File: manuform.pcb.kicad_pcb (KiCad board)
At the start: 2 copper layers, 89 x 94 mm, 45 parts, among them J1 Conn_01x05, J2 Conn_01x04, J3 Conn_01x01, J4 Conn_01x01, J5 Conn_01x01, SW1 SW_DIP_x01, SW2 SW_DIP_x01, SW3 SW_DIP_x01, SW4 SW_DIP_x01, SW5 SW_DIP_x01

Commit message: added gnd lugs
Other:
- board text added: "v0.0 Flatmax"
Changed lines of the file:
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@@
   (gr_line (start 189.5 28) (end 171.5 28)
     (stroke (width 0.05) (type default)) (layer "Edge.Cuts"))
+  (gr_text "v0.0\n\nFlatmax" (at 138 87.5 90) (layer "F.Cu")
+    (effects (font (size 1.5 1.5) (thickness 0.3) bold) (justify left bottom))
+  )
   (segment (start 154 59.38) (end 156 61.38) (width 0.2) (layer "F.Cu") (net 1))
   (segment (start 163 62.88) (end 164.5 61.38) (width 0.2) (layer "F.Cu") (net 1))

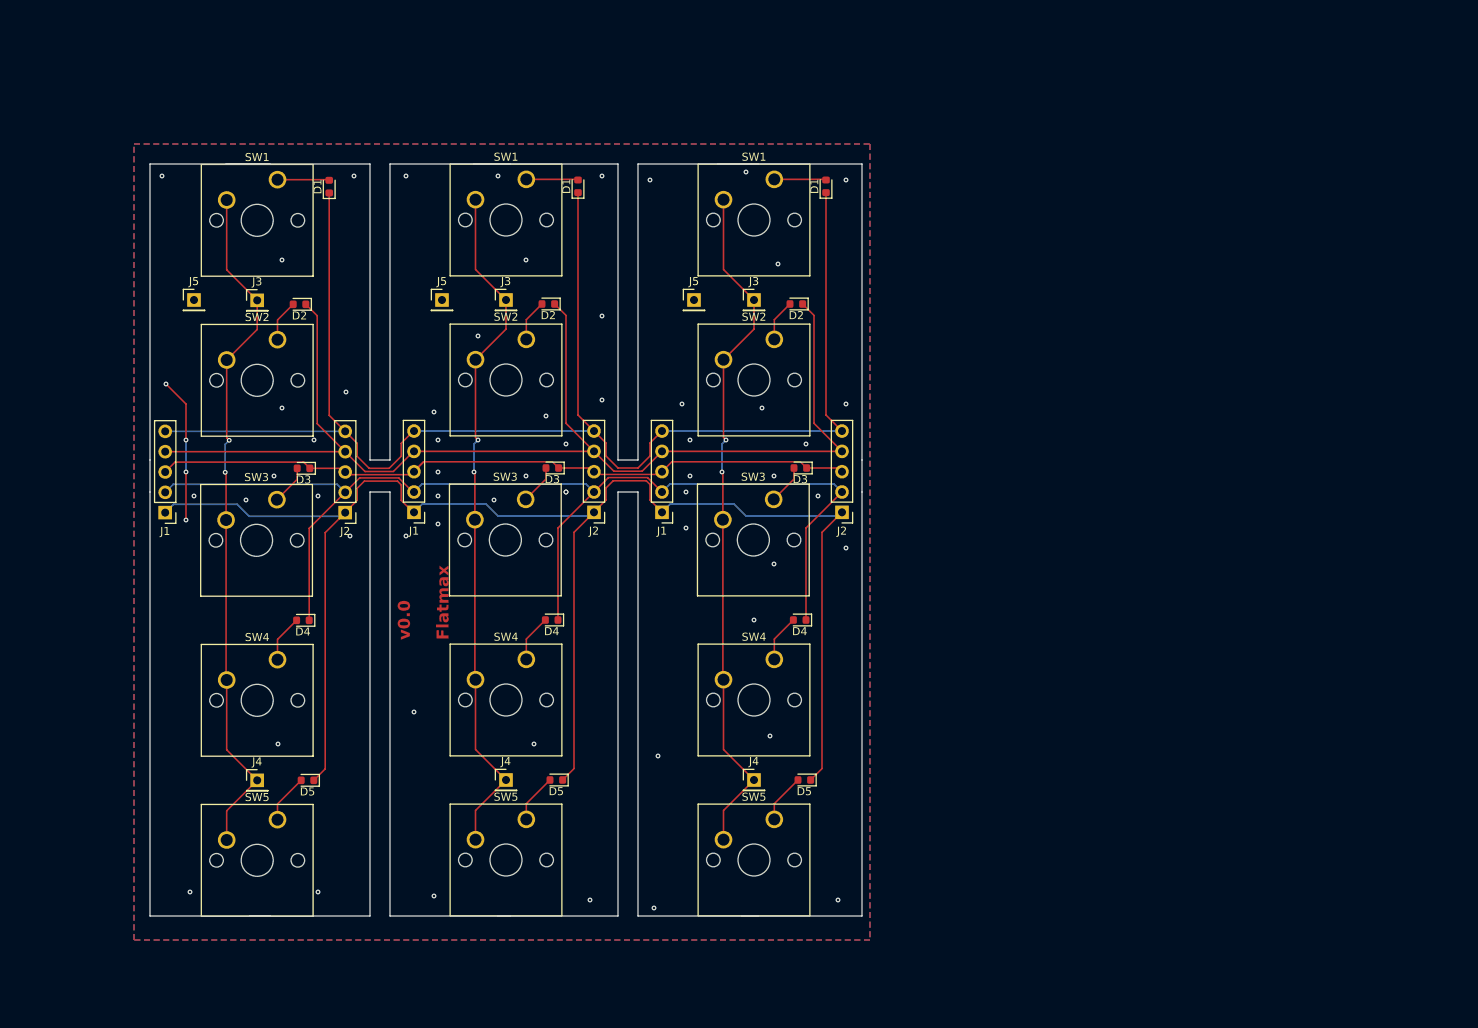
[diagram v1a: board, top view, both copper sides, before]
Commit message: increased separation to 25mm
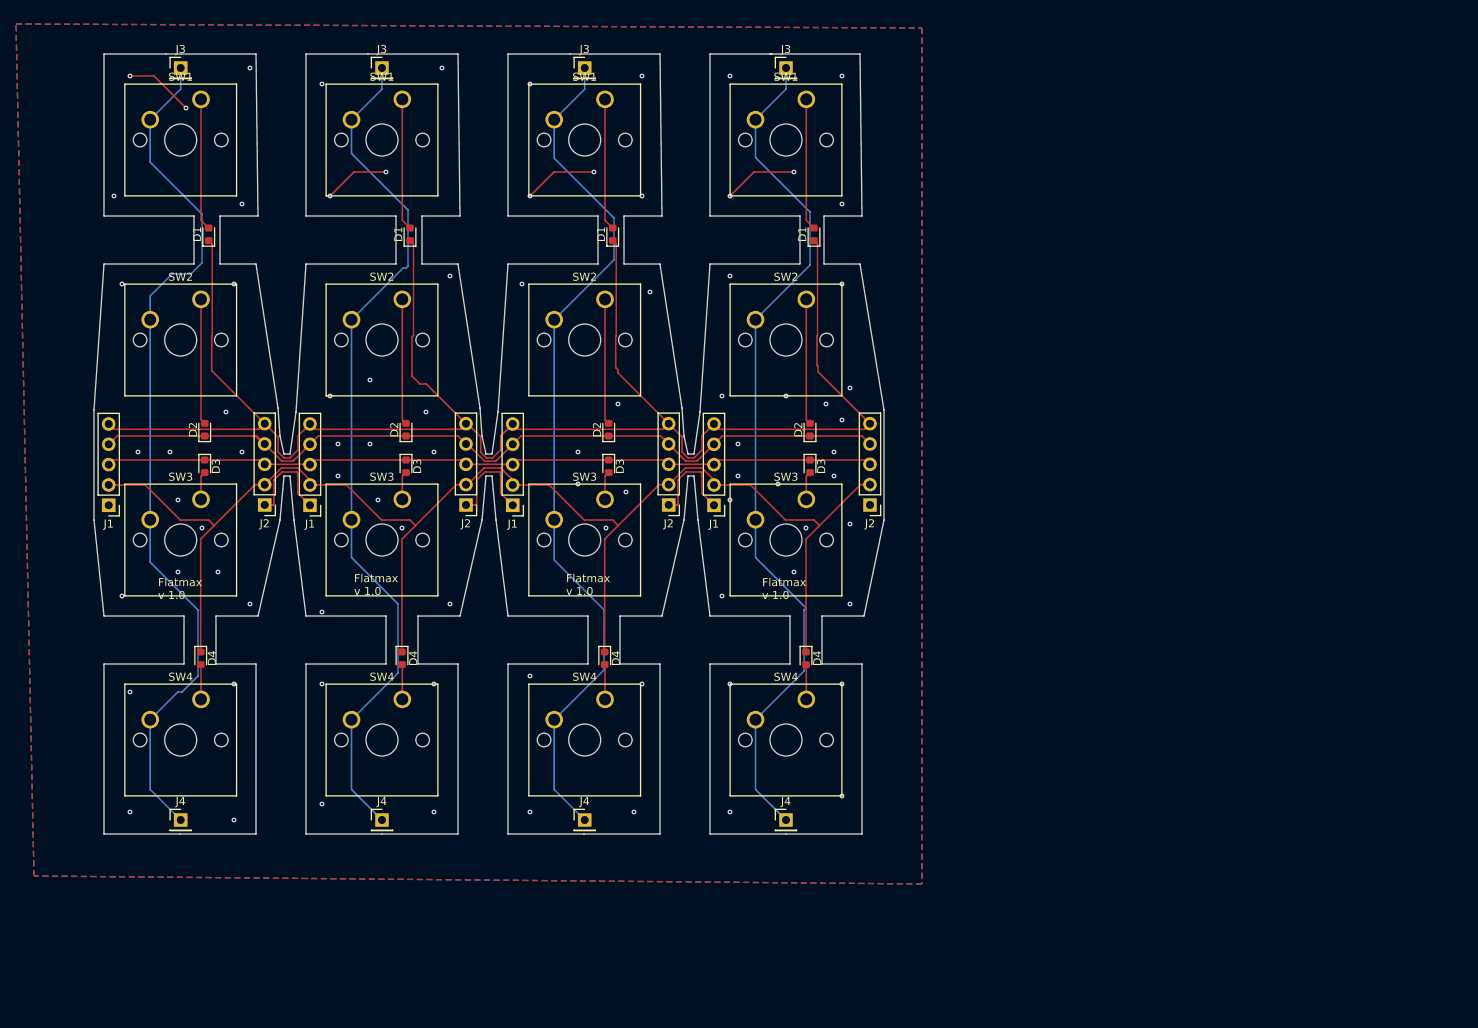
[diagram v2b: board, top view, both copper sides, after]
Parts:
- removed the D1 at (122.9, 30.8)
- removed the D1 at (185.0, 30.8)
- removed the D2 at (119.2, 45.5)
- removed the D2 at (181.3, 45.5)
- removed the D3 at (119.7, 66.0)
- removed the D3 at (181.8, 66.0)
- removed the D4 at (119.6, 85.0)
- removed the D4 at (181.7, 85.0)
- removed D5 (x3): D, Diode_SMD:D_0603_1608Metric
- removed the J1 at (164.5, 71.5)
- removed the J1 at (102.4, 71.6)
- removed the J2 at (124.9, 71.6)
- removed the J2 at (187.0, 71.5)
- removed the J3 at (176.0, 45.0)
- removed the J3 at (113.9, 45.0)
- removed the J4 at (176.0, 105.0)
- removed the J4 at (113.9, 105.0)
- removed J5 (x3): Conn_01x01, Connector_PinHeader_2.54mm:PinHeader_1x01_P2.54mm_Vertical
- removed the SW1 at (178.5, 29.9)
- removed the SW1 at (116.4, 30.0)
- removed the SW2 at (116.4, 50.0)
- removed the SW2 at (178.5, 49.9)
- removed the SW3 at (178.5, 69.9)
- removed the SW3 at (116.4, 70.0)
- removed the SW4 at (178.5, 89.9)
- removed the SW4 at (116.4, 90.0)
- removed SW5 (x3): SW_DIP_x01, Button_Switch_Keyboard:SW_Cherry_MX_1.00u_PCB
- added D1: D, Diode_SMD:D_0603_1608Metric, F.Cu at (133.0, 36.8)
- added D1: D, Diode_SMD:D_0603_1608Metric, F.Cu at (107.8, 36.8)
- added D1: D, Diode_SMD:D_0603_1608Metric, F.Cu at (158.3, 36.8)
- added D2: D, Diode_SMD:D_0603_1608Metric, F.Cu at (157.8, 61.2)
- added D2: D, Diode_SMD:D_0603_1608Metric, F.Cu at (107.3, 61.2)
- added D2: D, Diode_SMD:D_0603_1608Metric, F.Cu at (132.5, 61.2)
- added D3: D, Diode_SMD:D_0603_1608Metric, F.Cu at (107.3, 65.8)
- added D3: D, Diode_SMD:D_0603_1608Metric, F.Cu at (132.5, 65.8)
- added D3: D, Diode_SMD:D_0603_1608Metric, F.Cu at (157.8, 65.8)
- added D4: D, Diode_SMD:D_0603_1608Metric, F.Cu at (157.3, 89.8)
- added D4: D, Diode_SMD:D_0603_1608Metric, F.Cu at (132.0, 89.8)
- added D4: D, Diode_SMD:D_0603_1608Metric, F.Cu at (106.8, 89.8)
- added J1: Conn_01x05, Connector_PinHeader_2.54mm:PinHeader_1x05_P2.54mm_Vertical, F.Cu at (120.5, 70.7)
- added J1: Conn_01x05, Connector_PinHeader_2.54mm:PinHeader_1x05_P2.54mm_Vertical, F.Cu at (145.8, 70.7)
- added J1: Conn_01x05, Connector_PinHeader_2.54mm:PinHeader_1x05_P2.54mm_Vertical, F.Cu at (95.3, 70.7)
- added J2: Conn_01x04, Connector_PinHeader_2.54mm:PinHeader_1x05_P2.54mm_Vertical, F.Cu at (140.0, 70.6)
- added J2: Conn_01x04, Connector_PinHeader_2.54mm:PinHeader_1x05_P2.54mm_Vertical, F.Cu at (114.8, 70.6)
- added J2: Conn_01x04, Connector_PinHeader_2.54mm:PinHeader_1x05_P2.54mm_Vertical, F.Cu at (165.3, 70.6)
- added J3: Conn_01x01, Connector_PinHeader_2.54mm:PinHeader_1x01_P2.54mm_Vertical, F.Cu at (129.5, 16.0)
- added J3: Conn_01x01, Connector_PinHeader_2.54mm:PinHeader_1x01_P2.54mm_Vertical, F.Cu at (104.3, 16.0)
- added J3: Conn_01x01, Connector_PinHeader_2.54mm:PinHeader_1x01_P2.54mm_Vertical, F.Cu at (154.8, 16.0)
- added J4: Conn_01x01, Connector_PinHeader_2.54mm:PinHeader_1x01_P2.54mm_Vertical, F.Cu at (104.3, 110.0)
- added J4: Conn_01x01, Connector_PinHeader_2.54mm:PinHeader_1x01_P2.54mm_Vertical, F.Cu at (129.5, 110.0)
- added J4: Conn_01x01, Connector_PinHeader_2.54mm:PinHeader_1x01_P2.54mm_Vertical, F.Cu at (154.8, 110.0)
- added SW1: SW_DIP_x01, Button_Switch_Keyboard:SW_Cherry_MX_1.00u_PCB, F.Cu at (106.9, 19.9)
- added SW1: SW_DIP_x01, Button_Switch_Keyboard:SW_Cherry_MX_1.00u_PCB, F.Cu at (157.4, 19.9)
- added SW1: SW_DIP_x01, Button_Switch_Keyboard:SW_Cherry_MX_1.00u_PCB, F.Cu at (132.0, 19.9)
- added SW2: SW_DIP_x01, Button_Switch_Keyboard:SW_Cherry_MX_1.00u_PCB, F.Cu at (157.4, 44.9)
- added SW2: SW_DIP_x01, Button_Switch_Keyboard:SW_Cherry_MX_1.00u_PCB, F.Cu at (106.9, 44.9)
- added SW2: SW_DIP_x01, Button_Switch_Keyboard:SW_Cherry_MX_1.00u_PCB, F.Cu at (132.0, 44.9)
- added SW3: SW_DIP_x01, Button_Switch_Keyboard:SW_Cherry_MX_1.00u_PCB, F.Cu at (132.0, 69.9)
- added SW3: SW_DIP_x01, Button_Switch_Keyboard:SW_Cherry_MX_1.00u_PCB, F.Cu at (157.4, 69.9)
- added SW3: SW_DIP_x01, Button_Switch_Keyboard:SW_Cherry_MX_1.00u_PCB, F.Cu at (106.9, 69.9)
- added SW4: SW_DIP_x01, Button_Switch_Keyboard:SW_Cherry_MX_1.00u_PCB, F.Cu at (106.9, 94.9)
- added SW4: SW_DIP_x01, Button_Switch_Keyboard:SW_Cherry_MX_1.00u_PCB, F.Cu at (132.0, 94.9)
- added SW4: SW_DIP_x01, Button_Switch_Keyboard:SW_Cherry_MX_1.00u_PCB, F.Cu at (157.4, 94.9)
- moved J3 45.5 mm to (180.0, 16.0)
- moved J1 37.5 mm to (171.0, 70.7)
- moved SW1 36.4 mm to (182.5, 19.9)
- moved D2 36.3 mm to (183.0, 61.2), turned to 90 degrees
- moved J4 35.4 mm to (180.0, 110.0)
- moved SW2 35.4 mm to (182.5, 44.9)
- moved SW4 35.4 mm to (182.5, 94.9)
- moved SW3 35.1 mm to (182.5, 69.9)
- moved J2 34.5 mm to (190.5, 70.6)
- moved D3 32.2 mm to (183.0, 65.8), turned to -90 degrees
- moved D4 32.1 mm to (182.5, 89.8), turned to -90 degrees
- moved D1 30.1 mm to (183.5, 36.8)
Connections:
- J1 pad 1: Net-(D5-K) -> GND
- J2 pad 1: Net-(D5-K) -> GND
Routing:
- net Net-(D5-K): track 206.3 -> 0.00 mm
- net Net-(J3-Pin_1): track 260.2 -> 433.7 mm, vias 6 -> 0
- net GND: track 18.0 -> 72.5 mm, vias 62 -> 83
- net Net-(D2-A): track 15.7 -> 62.8 mm
- net Net-(D1-A): track 19.5 -> 65.9 mm
- net Net-(D2-K): track 150.0 -> 105.1 mm
- net Net-(D4-K): track 143.6 -> 184.2 mm
- net Net-(D1-K): track 187.9 -> 223.9 mm
- net Net-(D5-A): track 18.4 -> 0.00 mm
- net Net-(D3-K): track 89.9 -> 101.6 mm
- net Net-(D3-A): track 14.9 -> 14.1 mm
- net (no net): vias 0 -> 1
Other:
- board size 89 x 94 mm -> 98.8 x 97.5 mm
- board text added: "Flatmax v 1.0"
- board text removed: "v0.0 Flatmax"

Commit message: reduced the spacing, flipped switch fp horiz
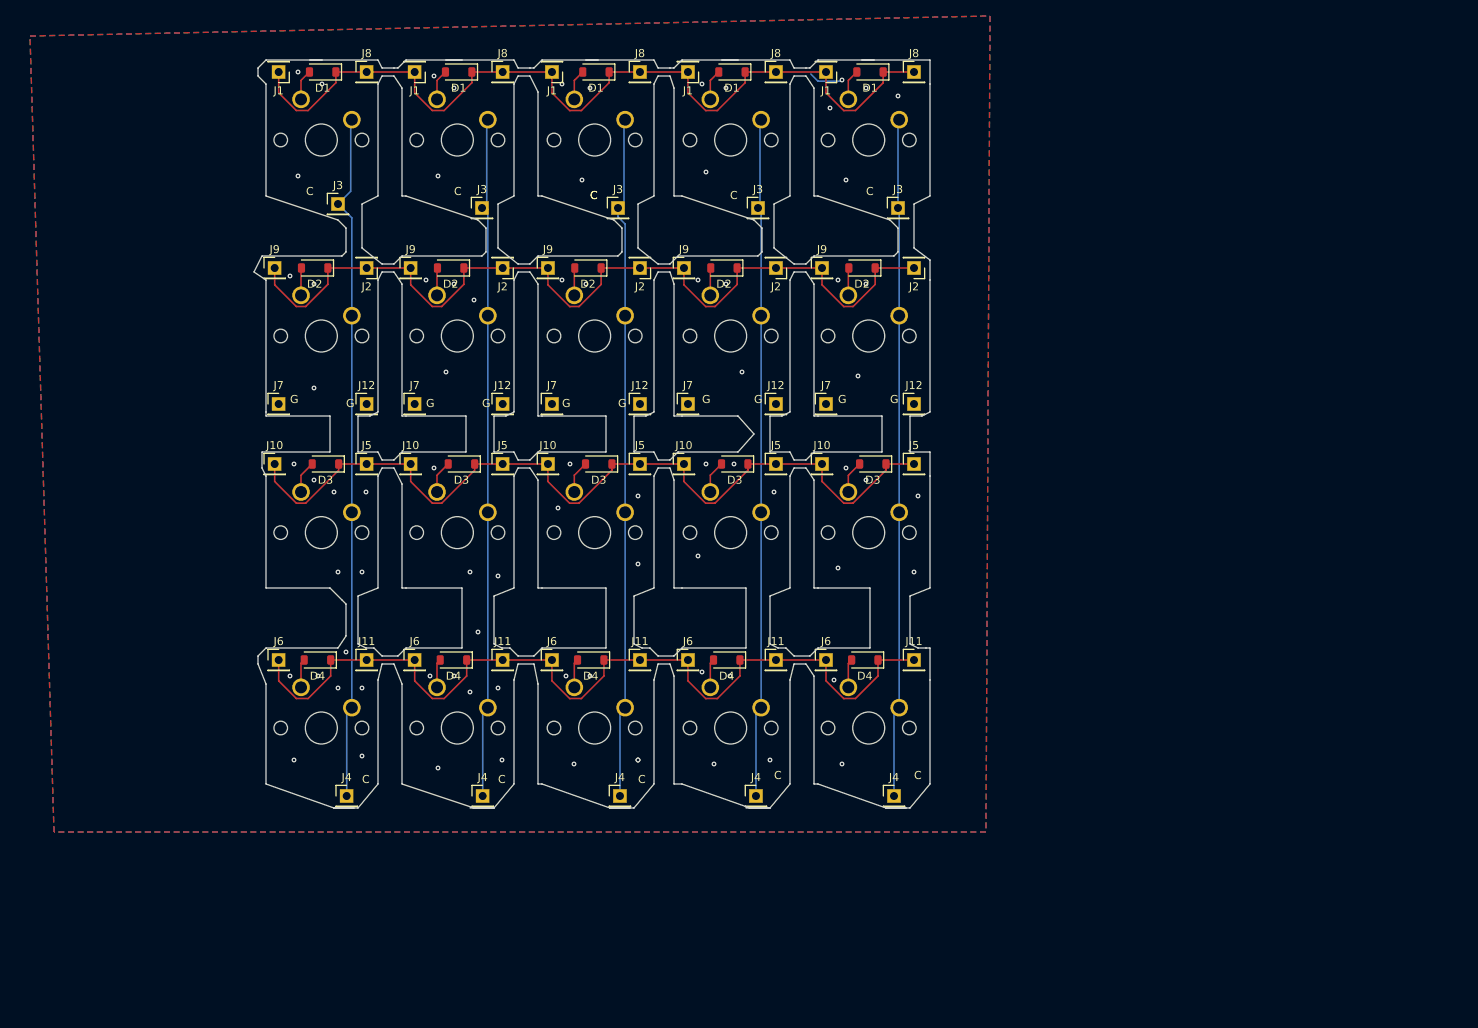
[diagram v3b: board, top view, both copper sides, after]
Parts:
- removed the D1 at (133.0, 36.8)
- removed the D1 at (107.8, 36.8)
- removed the D1 at (183.5, 36.8)
- removed the D1 at (158.3, 36.8)
- removed the D2 at (157.8, 61.2)
- removed the D2 at (183.0, 61.2)
- removed the D2 at (107.3, 61.2)
- removed the D2 at (132.5, 61.2)
- removed the D3 at (183.0, 65.8)
- removed the D3 at (107.3, 65.8)
- removed the D3 at (132.5, 65.8)
- removed the D3 at (157.8, 65.8)
- removed the D4 at (182.5, 89.8)
- removed the D4 at (157.3, 89.8)
- removed the D4 at (132.0, 89.8)
- removed the D4 at (106.8, 89.8)
- removed the J1 at (120.5, 70.7)
- removed the J1 at (171.0, 70.7)
- removed the J1 at (145.8, 70.7)
- removed the J1 at (95.3, 70.7)
- removed the J2 at (140.0, 70.6)
- removed the J2 at (114.8, 70.6)
- removed the J2 at (165.3, 70.6)
- removed the J2 at (190.5, 70.6)
- removed the J3 at (129.5, 16.0)
- removed the J3 at (104.3, 16.0)
- removed the J3 at (180.0, 16.0)
- removed the J3 at (154.8, 16.0)
- removed the J4 at (180.0, 110.0)
- removed the J4 at (104.3, 110.0)
- removed the J4 at (129.5, 110.0)
- removed the J4 at (154.8, 110.0)
- removed the SW1 at (106.9, 19.9)
- removed the SW1 at (157.4, 19.9)
- removed the SW1 at (182.5, 19.9)
- removed the SW1 at (132.0, 19.9)
- removed the SW2 at (157.4, 44.9)
- removed the SW2 at (106.9, 44.9)
- removed the SW2 at (132.0, 44.9)
- removed the SW2 at (182.5, 44.9)
- removed the SW3 at (132.0, 69.9)
- removed the SW3 at (157.4, 69.9)
- removed the SW3 at (182.5, 69.9)
- removed the SW3 at (106.9, 69.9)
- removed the SW4 at (106.9, 94.9)
- removed the SW4 at (132.0, 94.9)
- removed the SW4 at (157.4, 94.9)
- removed the SW4 at (182.5, 94.9)
- added D1: D, Diode_SMD:D_SOD-123, F.Cu at (122.1, 16.5)
- added D1: D, Diode_SMD:D_SOD-123, F.Cu at (139.1, 16.5)
- added D1: D, Diode_SMD:D_SOD-123, F.Cu at (156.2, 16.5)
- added D1: D, Diode_SMD:D_SOD-123, F.Cu at (190.5, 16.5)
- added D1: D, Diode_SMD:D_SOD-123, F.Cu at (173.2, 16.5)
- added D2: D, Diode_SMD:D_SOD-123, F.Cu at (172.2, 41.0)
- added D2: D, Diode_SMD:D_SOD-123, F.Cu at (121.1, 41.0)
- added D2: D, Diode_SMD:D_SOD-123, F.Cu at (138.1, 41.0)
- added D2: D, Diode_SMD:D_SOD-123, F.Cu at (155.2, 41.0)
- added D2: D, Diode_SMD:D_SOD-123, F.Cu at (189.5, 41.0)
- added D3: D, Diode_SMD:D_SOD-123, F.Cu at (122.4, 65.5)
- added D3: D, Diode_SMD:D_SOD-123, F.Cu at (173.6, 65.5)
- added D3: D, Diode_SMD:D_SOD-123, F.Cu at (139.4, 65.5)
- added D3: D, Diode_SMD:D_SOD-123, F.Cu at (190.8, 65.5)
- added D3: D, Diode_SMD:D_SOD-123, F.Cu at (156.6, 65.5)
- added D4: D, Diode_SMD:D_SOD-123, F.Cu at (172.6, 90.0)
- added D4: D, Diode_SMD:D_SOD-123, F.Cu at (121.4, 90.0)
- added D4: D, Diode_SMD:D_SOD-123, F.Cu at (138.4, 90.0)
- added D4: D, Diode_SMD:D_SOD-123, F.Cu at (155.6, 90.0)
- added D4: D, Diode_SMD:D_SOD-123, F.Cu at (189.8, 90.0)
- added J1: Conn_01x01_Pin, Connector_PinHeader_2.54mm:PinHeader_1x01_P2.54mm_Vertical, F.Cu at (150.7, 16.5)
- added J1: Conn_01x01_Pin, Connector_PinHeader_2.54mm:PinHeader_1x01_P2.54mm_Vertical, F.Cu at (116.6, 16.5)
- added J1: Conn_01x01_Pin, Connector_PinHeader_2.54mm:PinHeader_1x01_P2.54mm_Vertical, F.Cu at (185.0, 16.5)
- added J1: Conn_01x01_Pin, Connector_PinHeader_2.54mm:PinHeader_1x01_P2.54mm_Vertical, F.Cu at (167.7, 16.5)
- added J1: Conn_01x01_Pin, Connector_PinHeader_2.54mm:PinHeader_1x01_P2.54mm_Vertical, F.Cu at (133.6, 16.5)
- added J10: Conn_01x01_Pin, Connector_PinHeader_2.54mm:PinHeader_1x01_P2.54mm_Vertical, F.Cu at (133.1, 65.5)
- added J10: Conn_01x01_Pin, Connector_PinHeader_2.54mm:PinHeader_1x01_P2.54mm_Vertical, F.Cu at (116.1, 65.5)
- added J10: Conn_01x01_Pin, Connector_PinHeader_2.54mm:PinHeader_1x01_P2.54mm_Vertical, F.Cu at (167.2, 65.5)
- added J10: Conn_01x01_Pin, Connector_PinHeader_2.54mm:PinHeader_1x01_P2.54mm_Vertical, F.Cu at (150.2, 65.5)
- added J10: Conn_01x01_Pin, Connector_PinHeader_2.54mm:PinHeader_1x01_P2.54mm_Vertical, F.Cu at (184.5, 65.5)
- added J11: Conn_01x01_Pin, Connector_PinHeader_2.54mm:PinHeader_1x01_P2.54mm_Vertical, F.Cu at (178.7, 90.0)
- added J11: Conn_01x01_Pin, Connector_PinHeader_2.54mm:PinHeader_1x01_P2.54mm_Vertical, F.Cu at (161.7, 90.0)
- added J11: Conn_01x01_Pin, Connector_PinHeader_2.54mm:PinHeader_1x01_P2.54mm_Vertical, F.Cu at (127.6, 90.0)
- added J11: Conn_01x01_Pin, Connector_PinHeader_2.54mm:PinHeader_1x01_P2.54mm_Vertical, F.Cu at (196.0, 90.0)
- added J11: Conn_01x01_Pin, Connector_PinHeader_2.54mm:PinHeader_1x01_P2.54mm_Vertical, F.Cu at (144.6, 90.0)
- added J12: Conn_01x01_Pin, Connector_PinHeader_2.54mm:PinHeader_1x01_P2.54mm_Vertical, F.Cu at (127.6, 58.0)
- added J12: Conn_01x01_Pin, Connector_PinHeader_2.54mm:PinHeader_1x01_P2.54mm_Vertical, F.Cu at (161.7, 58.0)
- added J12: Conn_01x01_Pin, Connector_PinHeader_2.54mm:PinHeader_1x01_P2.54mm_Vertical, F.Cu at (178.7, 58.0)
- added J12: Conn_01x01_Pin, Connector_PinHeader_2.54mm:PinHeader_1x01_P2.54mm_Vertical, F.Cu at (196.0, 58.0)
- added J12: Conn_01x01_Pin, Connector_PinHeader_2.54mm:PinHeader_1x01_P2.54mm_Vertical, F.Cu at (144.6, 58.0)
- added J2: Conn_01x01_Pin, Connector_PinHeader_2.54mm:PinHeader_1x01_P2.54mm_Vertical, F.Cu at (127.6, 41.0)
- added J2: Conn_01x01_Pin, Connector_PinHeader_2.54mm:PinHeader_1x01_P2.54mm_Vertical, F.Cu at (196.0, 41.0)
- added J2: Conn_01x01_Pin, Connector_PinHeader_2.54mm:PinHeader_1x01_P2.54mm_Vertical, F.Cu at (144.6, 41.0)
- added J2: Conn_01x01_Pin, Connector_PinHeader_2.54mm:PinHeader_1x01_P2.54mm_Vertical, F.Cu at (161.7, 41.0)
- added J2: Conn_01x01_Pin, Connector_PinHeader_2.54mm:PinHeader_1x01_P2.54mm_Vertical, F.Cu at (178.7, 41.0)
- added J3: Conn_01x01, Connector_PinHeader_2.54mm:PinHeader_1x01_P2.54mm_Vertical, F.Cu at (159.0, 33.5)
- added J3: Conn_01x01, Connector_PinHeader_2.54mm:PinHeader_1x01_P2.54mm_Vertical, F.Cu at (124.0, 33.0)
- added J3: Conn_01x01, Connector_PinHeader_2.54mm:PinHeader_1x01_P2.54mm_Vertical, F.Cu at (142.0, 33.5)
- added J3: Conn_01x01, Connector_PinHeader_2.54mm:PinHeader_1x01_P2.54mm_Vertical, F.Cu at (176.5, 33.5)
- added J3: Conn_01x01, Connector_PinHeader_2.54mm:PinHeader_1x01_P2.54mm_Vertical, F.Cu at (194.0, 33.5)
- added J4: Conn_01x01, Connector_PinHeader_2.54mm:PinHeader_1x01_P2.54mm_Vertical, F.Cu at (176.2, 107.0)
- added J4: Conn_01x01, Connector_PinHeader_2.54mm:PinHeader_1x01_P2.54mm_Vertical, F.Cu at (159.2, 107.0)
- added J4: Conn_01x01, Connector_PinHeader_2.54mm:PinHeader_1x01_P2.54mm_Vertical, F.Cu at (142.1, 107.0)
- added J4: Conn_01x01, Connector_PinHeader_2.54mm:PinHeader_1x01_P2.54mm_Vertical, F.Cu at (193.5, 107.0)
- added J4: Conn_01x01, Connector_PinHeader_2.54mm:PinHeader_1x01_P2.54mm_Vertical, F.Cu at (125.1, 107.0)
- added J5: Conn_01x01_Pin, Connector_PinHeader_2.54mm:PinHeader_1x01_P2.54mm_Vertical, F.Cu at (161.7, 65.5)
- added J5: Conn_01x01_Pin, Connector_PinHeader_2.54mm:PinHeader_1x01_P2.54mm_Vertical, F.Cu at (144.6, 65.5)
- added J5: Conn_01x01_Pin, Connector_PinHeader_2.54mm:PinHeader_1x01_P2.54mm_Vertical, F.Cu at (127.6, 65.5)
- added J5: Conn_01x01_Pin, Connector_PinHeader_2.54mm:PinHeader_1x01_P2.54mm_Vertical, F.Cu at (178.7, 65.5)
- added J5: Conn_01x01_Pin, Connector_PinHeader_2.54mm:PinHeader_1x01_P2.54mm_Vertical, F.Cu at (196.0, 65.5)
- added J6: Conn_01x01_Pin, Connector_PinHeader_2.54mm:PinHeader_1x01_P2.54mm_Vertical, F.Cu at (150.7, 90.0)
- added J6: Conn_01x01_Pin, Connector_PinHeader_2.54mm:PinHeader_1x01_P2.54mm_Vertical, F.Cu at (185.0, 90.0)
- added J6: Conn_01x01_Pin, Connector_PinHeader_2.54mm:PinHeader_1x01_P2.54mm_Vertical, F.Cu at (167.7, 90.0)
- added J6: Conn_01x01_Pin, Connector_PinHeader_2.54mm:PinHeader_1x01_P2.54mm_Vertical, F.Cu at (116.6, 90.0)
- added J6: Conn_01x01_Pin, Connector_PinHeader_2.54mm:PinHeader_1x01_P2.54mm_Vertical, F.Cu at (133.6, 90.0)
- added J7: Conn_01x01_Pin, Connector_PinHeader_2.54mm:PinHeader_1x01_P2.54mm_Vertical, F.Cu at (150.7, 58.0)
- added J7: Conn_01x01_Pin, Connector_PinHeader_2.54mm:PinHeader_1x01_P2.54mm_Vertical, F.Cu at (133.6, 58.0)
- added J7: Conn_01x01_Pin, Connector_PinHeader_2.54mm:PinHeader_1x01_P2.54mm_Vertical, F.Cu at (167.7, 58.0)
- added J7: Conn_01x01_Pin, Connector_PinHeader_2.54mm:PinHeader_1x01_P2.54mm_Vertical, F.Cu at (116.6, 58.0)
- added J7: Conn_01x01_Pin, Connector_PinHeader_2.54mm:PinHeader_1x01_P2.54mm_Vertical, F.Cu at (185.0, 58.0)
- added J8: Conn_01x01_Pin, Connector_PinHeader_2.54mm:PinHeader_1x01_P2.54mm_Vertical, F.Cu at (144.6, 16.5)
- added J8: Conn_01x01_Pin, Connector_PinHeader_2.54mm:PinHeader_1x01_P2.54mm_Vertical, F.Cu at (127.6, 16.5)
- added J8: Conn_01x01_Pin, Connector_PinHeader_2.54mm:PinHeader_1x01_P2.54mm_Vertical, F.Cu at (161.7, 16.5)
- added J8: Conn_01x01_Pin, Connector_PinHeader_2.54mm:PinHeader_1x01_P2.54mm_Vertical, F.Cu at (196.0, 16.5)
- added J8: Conn_01x01_Pin, Connector_PinHeader_2.54mm:PinHeader_1x01_P2.54mm_Vertical, F.Cu at (178.7, 16.5)
- added J9: Conn_01x01_Pin, Connector_PinHeader_2.54mm:PinHeader_1x01_P2.54mm_Vertical, F.Cu at (167.2, 41.0)
- added J9: Conn_01x01_Pin, Connector_PinHeader_2.54mm:PinHeader_1x01_P2.54mm_Vertical, F.Cu at (184.5, 41.0)
- added J9: Conn_01x01_Pin, Connector_PinHeader_2.54mm:PinHeader_1x01_P2.54mm_Vertical, F.Cu at (150.2, 41.0)
- added J9: Conn_01x01_Pin, Connector_PinHeader_2.54mm:PinHeader_1x01_P2.54mm_Vertical, F.Cu at (116.1, 41.0)
- added J9: Conn_01x01_Pin, Connector_PinHeader_2.54mm:PinHeader_1x01_P2.54mm_Vertical, F.Cu at (133.1, 41.0)
- added SW1: SW_DIP_x01, Button_Switch_Keyboard:SW_Cherry_MX_1.00u_PCB, B.Cu at (153.5, 19.9)
- added SW1: SW_DIP_x01, Button_Switch_Keyboard:SW_Cherry_MX_1.00u_PCB, B.Cu at (136.4, 19.9)
- added SW1: SW_DIP_x01, Button_Switch_Keyboard:SW_Cherry_MX_1.00u_PCB, B.Cu at (187.8, 19.9)
- added SW1: SW_DIP_x01, Button_Switch_Keyboard:SW_Cherry_MX_1.00u_PCB, B.Cu at (119.4, 19.9)
- added SW1: SW_DIP_x01, Button_Switch_Keyboard:SW_Cherry_MX_1.00u_PCB, B.Cu at (170.5, 19.9)
- added SW2: SW_DIP_x01, Button_Switch_Keyboard:SW_Cherry_MX_1.00u_PCB, B.Cu at (119.4, 44.4)
- added SW2: SW_DIP_x01, Button_Switch_Keyboard:SW_Cherry_MX_1.00u_PCB, B.Cu at (136.4, 44.4)
- added SW2: SW_DIP_x01, Button_Switch_Keyboard:SW_Cherry_MX_1.00u_PCB, B.Cu at (170.5, 44.4)
- added SW2: SW_DIP_x01, Button_Switch_Keyboard:SW_Cherry_MX_1.00u_PCB, B.Cu at (187.8, 44.4)
- added SW2: SW_DIP_x01, Button_Switch_Keyboard:SW_Cherry_MX_1.00u_PCB, B.Cu at (153.5, 44.4)
- added SW3: SW_DIP_x01, Button_Switch_Keyboard:SW_Cherry_MX_1.00u_PCB, B.Cu at (119.4, 69.0)
- added SW3: SW_DIP_x01, Button_Switch_Keyboard:SW_Cherry_MX_1.00u_PCB, B.Cu at (187.8, 69.0)
- added SW3: SW_DIP_x01, Button_Switch_Keyboard:SW_Cherry_MX_1.00u_PCB, B.Cu at (136.4, 69.0)
- added SW3: SW_DIP_x01, Button_Switch_Keyboard:SW_Cherry_MX_1.00u_PCB, B.Cu at (170.5, 69.0)
- added SW3: SW_DIP_x01, Button_Switch_Keyboard:SW_Cherry_MX_1.00u_PCB, B.Cu at (153.5, 69.0)
- added SW4: SW_DIP_x01, Button_Switch_Keyboard:SW_Cherry_MX_1.00u_PCB, B.Cu at (119.4, 93.4)
- added SW4: SW_DIP_x01, Button_Switch_Keyboard:SW_Cherry_MX_1.00u_PCB, B.Cu at (170.5, 93.4)
- added SW4: SW_DIP_x01, Button_Switch_Keyboard:SW_Cherry_MX_1.00u_PCB, B.Cu at (153.5, 93.4)
- added SW4: SW_DIP_x01, Button_Switch_Keyboard:SW_Cherry_MX_1.00u_PCB, B.Cu at (187.8, 93.4)
- added SW4: SW_DIP_x01, Button_Switch_Keyboard:SW_Cherry_MX_1.00u_PCB, B.Cu at (136.4, 93.4)
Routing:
- net Net-(D1-K): track 223.9 -> 111.0 mm
- net Net-(D4-K): track 184.2 -> 112.9 mm
- net GND: track 72.5 -> 4.33 mm, vias 83 -> 79
- net Net-(D1-A): track 65.9 -> 19.3 mm
- net Net-(D2-A): track 62.8 -> 17.2 mm
- net Net-(J3-Pin_1): track 433.7 -> 426.3 mm
- net Net-(D3-K): track 101.6 -> 108.9 mm
- net Net-(D2-K): track 105.1 -> 112.0 mm
- net Net-(D3-A): track 14.1 -> 20.4 mm
- net (no net): vias 1 -> 0
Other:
- board size 98.8 x 97.5 mm -> 84.5 x 93.5 mm
- board text added: "C"
- board text added: "G"
- board text removed: "Flatmax v 1.0"
